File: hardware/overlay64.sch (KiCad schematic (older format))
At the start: 17 parts, among them IC1 ATMEGA328P-P, P1 ISP, P2 MAIN, P3 INPUT/BYPASS, Q1 BC547B, U1 LM1881, Y1 20MHz

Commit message: Hardware: Rearranged components, rerouting...
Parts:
- removed P3: INPUT/BYPASS, Pin_Headers:Pin_Header_Straight_2x14, symbol CONN_02X14
- added P3: CONTROL, Pin_Headers:Pin_Header_Angled_1x02, symbol CONN_01X02
- added P4: BYPASS, Pin_Headers:Pin_Header_Angled_1x12, symbol CONN_01X12
- added P5: INPUT, Pin_Headers:Pin_Header_Angled_1x12, symbol CONN_01X12
- P2: footprint Pin_Headers:Pin_Header_Straight_1x03 -> Pin_Headers:Pin_Header_Angled_1x03
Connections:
- net IN0: now also P4.1 (P1), P5.12 (P12)
- net IN1: now also P4.2 (P2), P5.11 (P11)
- net IN10: now also P4.11 (P11), P5.2 (P2)
- net IN11: now also P4.12 (P12), P5.1 (P1)
- net IN2: now also P4.3 (P3), P5.10 (P10)
- net IN3: now also P4.4 (P4), P5.9 (P9)
- net IN4: now also P4.5 (P5), P5.8 (P8)
- net IN5: now also P4.6 (P6), P5.7 (P7)
- net IN6: now also P4.7 (P7), P5.6 (P6)
- net IN7: now also P4.8 (P8), P5.5 (P5)
- net IN8: now also P4.9 (P9), P5.4 (P4)
- net IN9: now also P4.10 (P10), P5.3 (P3)
- net ~OE: now also P3.1 (P1)
- net ~OR: now also P3.2 (P2)
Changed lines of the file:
@@
 $EndComp
 $Comp
-L PWR_FLAG #FLG1
+L PWR_FLAG #FLG01
 U 1 1 56A1EF0B
 P 6250 7500
-F 0 "#FLG1" H 6250 7595 50  0001 C CNN
+F 0 "#FLG01" H 6250 7595 50  0001 C CNN
 F 1 "PWR_FLAG" H 6250 7680 50  0000 C CNN
 F 2 "" H 6250 7500 60  0000 C CNN
@@
 $EndComp
 $Comp
-L VCC #PWR12
+L VCC #PWR02
 U 1 1 56A1EF40
 P 6250 7500
-F 0 "#PWR12" H 6250 7350 50  0001 C CNN
+F 0 "#PWR02" H 6250 7350 50  0001 C CNN
 F 1 "VCC" H 6250 7650 50  0000 C CNN
 F 2 "" H 6250 7500 60  0000 C CNN
@@
 $EndComp
 $Comp
-L PWR_FLAG #FLG2
+L PWR_FLAG #FLG03
 U 1 1 56A1EF56
 P 6700 7500
-F 0 "#FLG2" H 6700 7595 50  0001 C CNN
+F 0 "#FLG03" H 6700 7595 50  0001 C CNN
 F 1 "PWR_FLAG" H 6700 7680 50  0000 C CNN
 F 2 "" H 6700 7500 60  0000 C CNN
@@
 $EndComp
 $Comp
-L GND #PWR15
+L GND #PWR04
 U 1 1 56A1EF6C
 P 6700 7500
-F 0 "#PWR15" H 6700 7250 50  0001 C CNN
+F 0 "#PWR04" H 6700 7250 50  0001 C CNN
 F 1 "GND" H 6700 7350 50  0000 C CNN
 F 2 "" H 6700 7500 60  0000 C CNN
@@
 $EndComp
 $Comp
-L VCC #PWR9
+L VCC #PWR05
 U 1 1 56A1F13D
 P 5600 4850
-F 0 "#PWR9" H 5600 4700 50  0001 C CNN
+F 0 "#PWR05" H 5600 4700 50  0001 C CNN
 F 1 "VCC" H 5600 5000 50  0000 C CNN
 F 2 "" H 5600 4850 60  0000 C CNN
@@
 $EndComp
 $Comp
-L GND #PWR10
+L GND #PWR06
 U 1 1 56A1F155
 P 5600 5150
-F 0 "#PWR10" H 5600 4900 50  0001 C CNN
+F 0 "#PWR06" H 5600 4900 50  0001 C CNN
 F 1 "GND" H 5600 5000 50  0000 C CNN
 F 2 "" H 5600 5150 60  0000 C CNN
@@
 $EndComp
 $Comp
-L GND #PWR2
+L GND #PWR07
 U 1 1 56A1F1BC
 P 2050 2800
-F 0 "#PWR2" H 2050 2550 50  0001 C CNN
+F 0 "#PWR07" H 2050 2550 50  0001 C CNN
 F 1 "GND" H 2050 2650 50  0000 C CNN
 F 2 "" H 2050 2800 60  0000 C CNN
@@
 $EndComp
 $Comp
-L GND #PWR16
+L GND #PWR08
 U 1 1 56A1F3BB
 P 6850 4350
-F 0 "#PWR16" H 6850 4100 50  0001 C CNN
+F 0 "#PWR08" H 6850 4100 50  0001 C CNN
 F 1 "GND" H 6850 4200 50  0000 C CNN
 F 2 "" H 6850 4350 60  0000 C CNN
@@
 $EndComp
 $Comp
-L VCC #PWR1
+L VCC #PWR09
 U 1 1 56A1FF3A
 P 2000 2500
-F 0 "#PWR1" H 2000 2350 50  0001 C CNN
+F 0 "#PWR09" H 2000 2350 50  0001 C CNN
 F 1 "VCC" H 2000 2650 50  0000 C CNN
 F 2 "" H 2000 2500 60  0000 C CNN
@@
 $EndComp
 $Comp
-L GND #PWR3
+L GND #PWR010
 U 1 1 56A20155
 P 2450 4700
-F 0 "#PWR3" H 2450 4450 50  0001 C CNN
+F 0 "#PWR010" H 2450 4450 50  0001 C CNN
 F 1 "GND" H 2450 4550 50  0000 C CNN
 F 2 "" H 2450 4700 60  0000 C CNN
@@
 $EndComp
 $Comp
-L GND #PWR4
+L GND #PWR011
 U 1 1 56A60DBD
 P 2450 4800
-F 0 "#PWR4" H 2450 4550 50  0001 C CNN
+F 0 "#PWR011" H 2450 4550 50  0001 C CNN
 F 1 "GND" H 2450 4650 50  0000 C CNN
 F 2 "" H 2450 4800 60  0000 C CNN
@@
 Connection ~ 6850 4350
 $Comp
-L VCC #PWR11
+L VCC #PWR012
 U 1 1 56A78618
 P 5800 2600
-F 0 "#PWR11" H 5800 2450 50  0001 C CNN
+F 0 "#PWR012" H 5800 2450 50  0001 C CNN
 F 1 "VCC" H 5800 2750 50  0000 C CNN
 F 2 "" H 5800 2600 60  0000 C CNN
@@
 MOSI
 $Comp
-L VCC #PWR5
+L VCC #PWR013
 U 1 1 56A92B5A
 P 3750 1750
-F 0 "#PWR5" H 3750 1600 50  0001 C CNN
+F 0 "#PWR013" H 3750 1600 50  0001 C CNN
 F 1 "VCC" H 3750 1900 50  0000 C CNN
 F 2 "" H 3750 1750 60  0000 C CNN
@@
 $EndComp
 $Comp
-L GND #PWR6
+L GND #PWR014
 U 1 1 56A92BBD
 P 3750 1950
-F 0 "#PWR6" H 3750 1700 50  0001 C CNN
+F 0 "#PWR014" H 3750 1700 50  0001 C CNN
 F 1 "GND" H 3750 1800 50  0000 C CNN
 F 2 "" H 3750 1950 60  0000 C CNN
@@
 $EndComp
 $Comp
-L GND #PWR7
+L GND #PWR015
 U 1 1 56A976F1
 P 4850 3050
-F 0 "#PWR7" H 4850 2800 50  0001 C CNN
+F 0 "#PWR015" H 4850 2800 50  0001 C CNN
 F 1 "GND" H 4850 2900 50  0000 C CNN
 F 2 "" H 4850 3050 60  0000 C CNN
@@
 $EndComp
 $Comp
-L GND #PWR8
+L GND #PWR016
 U 1 1 56A97733
 P 4850 3250
-F 0 "#PWR8" H 4850 3000 50  0001 C CNN
+F 0 "#PWR016" H 4850 3000 50  0001 C CNN
 F 1 "GND" H 4850 3100 50  0000 C CNN
 F 2 "" H 4850 3250 60  0000 C CNN
@@
 F 0 "P2" H 6650 3750 50  0000 C CNN
 F 1 "MAIN" V 6750 3550 50  0000 C CNN
-F 2 "Pin_Headers:Pin_Header_Straight_1x03" H 6650 3550 60  0001 C CNN
+F 2 "Pin_Headers:Pin_Header_Angled_1x03" H 6650 3550 60  0001 C CNN
 F 3 "" H 6650 3550 60  0000 C CNN
 	1    6650 3550
@@
 $EndComp
 $Comp
-L VCC #PWR13
+L VCC #PWR017
 U 1 1 56A9E7D0
 P 6450 3450
-F 0 "#PWR13" H 6450 3300 50  0001 C CNN
+F 0 "#PWR017" H 6450 3300 50  0001 C CNN
 F 1 "VCC" H 6450 3600 50  0000 C CNN
 F 2 "" H 6450 3450 60  0000 C CNN
@@
 $EndComp
 $Comp
-L GND #PWR14
+L GND #PWR018
 U 1 1 56A9E875
 P 6450 3650
-F 0 "#PWR14" H 6450 3400 50  0001 C CNN
+F 0 "#PWR018" H 6450 3400 50  0001 C CNN
 F 1 "GND" H 6450 3500 50  0000 C CNN
 F 2 "" H 6450 3650 60  0000 C CNN
@@
 Wire Wire Line
 	4750 4450 5300 4450
-Text Label 7750 3100 2    60   ~ 0
+Text Label 8700 3100 2    60   ~ 0
 IN0
-Text Label 7750 3200 2    60   ~ 0
+Text Label 8700 3200 2    60   ~ 0
 IN1
-Text Label 7750 3300 2    60   ~ 0
+Text Label 8700 3300 2    60   ~ 0
 IN2
-Text Label 7750 3400 2    60   ~ 0
+Text Label 8700 3400 2    60   ~ 0
 IN3
-Text Label 7750 3500 2    60   ~ 0
+Text Label 8700 3500 2    60   ~ 0
 IN4
-Text Label 7750 3600 2    60   ~ 0
+Text Label 8700 3600 2    60   ~ 0
 IN5
-Text Label 7750 3700 2    60   ~ 0
+Text Label 8700 3700 2    60   ~ 0
 IN6
-Text Label 7750 3800 2    60   ~ 0
+Text Label 8700 3800 2    60   ~ 0
 IN7
-Text Label 7750 3900 2    60   ~ 0
+Text Label 8700 3900 2    60   ~ 0
 IN8
-Text Label 7750 4000 2    60   ~ 0
+Text Label 8700 4000 2    60   ~ 0
 IN9
-Text Label 7750 4100 2    60   ~ 0
+Text Label 8700 4100 2    60   ~ 0
 IN10
-Text Label 7750 4200 2    60   ~ 0
+Text Label 8700 4200 2    60   ~ 0
 IN11
 $Comp
@@
 Text Label 4350 4800 0    60   ~ 0
 ~OR
-Text Label 7750 4300 2    60   ~ 0
+Text Label 4300 6150 2    60   ~ 0
 ~OE
 Text Label 6150 3550 0    60   ~ 0
 LUMA
-$Comp
-L CONN_02X14 P3
-U 1 1 56B0DCD2
-P 8000 3750
-F 0 "P3" H 8000 4500 50  0000 C CNN
-F 1 "INPUT/BYPASS" V 8000 3750 50  0000 C CNN
-F 2 "Pin_Headers:Pin_Header_Straight_2x14" H 8000 2600 60  0001 C CNN
-F 3 "" H 8000 2600 60  0000 C CNN
-	1    8000 3750
-	1    0    0    -1
-$EndComp
-Text Label 8250 4300 0    60   ~ 0
-~OE
-Text Label 8250 3100 0    60   ~ 0
+Text Label 7850 3150 2    60   ~ 0
 IN0
-Text Label 8250 3200 0    60   ~ 0
+Text Label 7850 3250 2    60   ~ 0
 IN1
-Text Label 8250 3300 0    60   ~ 0
+Text Label 7850 3350 2    60   ~ 0
 IN2
-Text Label 8250 3400 0    60   ~ 0
+Text Label 7850 3450 2    60   ~ 0
 IN3
-Text Label 8250 3500 0    60   ~ 0
+Text Label 7850 3550 2    60   ~ 0
 IN4
-Text Label 8250 3600 0    60   ~ 0
+Text Label 7850 3650 2    60   ~ 0
 IN5
-Text Label 8250 3700 0    60   ~ 0
+Text Label 7850 3750 2    60   ~ 0
 IN6
-Text Label 8250 3800 0    60   ~ 0
+Text Label 7850 3850 2    60   ~ 0
 IN7
-Text Label 8250 3900 0    60   ~ 0
+Text Label 7850 3950 2    60   ~ 0
 IN8
-Text Label 8250 4000 0    60   ~ 0
+Text Label 7850 4050 2    60   ~ 0
 IN9
-Text Label 8250 4100 0    60   ~ 0
+Text Label 7850 4150 2    60   ~ 0
 IN10
-Text Label 8250 4200 0    60   ~ 0
+Text Label 7850 4250 2    60   ~ 0
 IN11
 $Comp
@@
 Text Label 4350 4700 0    60   ~ 0
 ~OE
-Text Label 8250 4400 0    60   ~ 0
+Text Label 4300 6250 2    60   ~ 0
 ~OR
-Text Label 7750 4400 2    60   ~ 0
-~OR
+$Comp
+L CONN_01X12 P4
+U 1 1 572F57F1
+P 8900 3650
+F 0 "P4" H 8900 4300 50  0000 C CNN
+F 1 "BYPASS" V 9000 3650 50  0000 C CNN
+F 2 "Pin_Headers:Pin_Header_Angled_1x12" H 8900 3650 50  0001 C CNN
+F 3 "" H 8900 3650 50  0000 C CNN
+	1    8900 3650
+	1    0    0    -1
+$EndComp
+$Comp
+L CONN_01X12 P5
+U 1 1 572F58A5
+P 8050 3700
+F 0 "P5" H 8050 4350 50  0000 C CNN
+F 1 "INPUT" V 8150 3700 50  0000 C CNN
+F 2 "Pin_Headers:Pin_Header_Angled_1x12" H 8050 3700 50  0001 C CNN
+F 3 "" H 8050 3700 50  0000 C CNN
+	1    8050 3700
+	1    0    0    1
+$EndComp
+$Comp
+L CONN_01X02 P3
+U 1 1 572F59E5
+P 4500 6200
+F 0 "P3" H 4500 6350 50  0000 C CNN
+F 1 "CONTROL" V 4600 6200 50  0000 C CNN
+F 2 "Pin_Headers:Pin_Header_Angled_1x02" H 4500 6200 50  0001 C CNN
+F 3 "" H 4500 6200 50  0000 C CNN
+	1    4500 6200
+	1    0    0    -1
+$EndComp
 $EndSCHEMATC

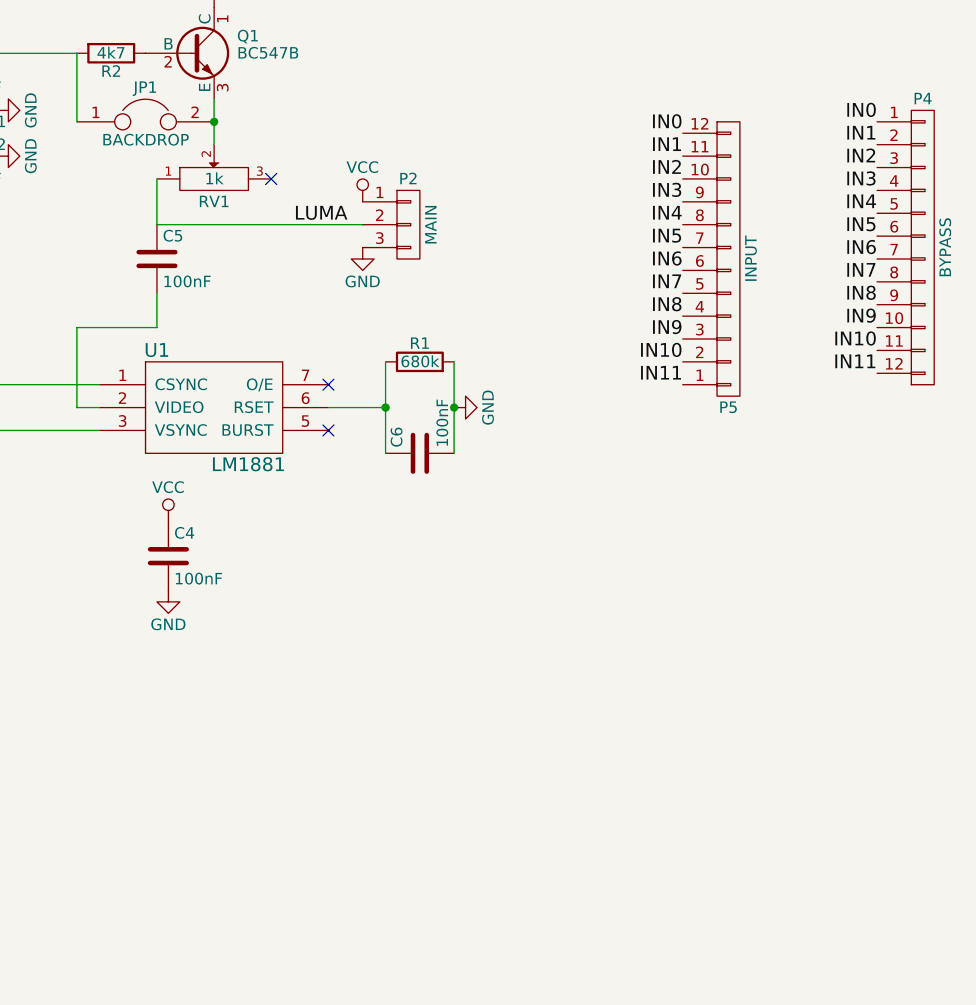
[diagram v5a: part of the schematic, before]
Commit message: Hardware: Fixed orientation/wiring for brightness pot
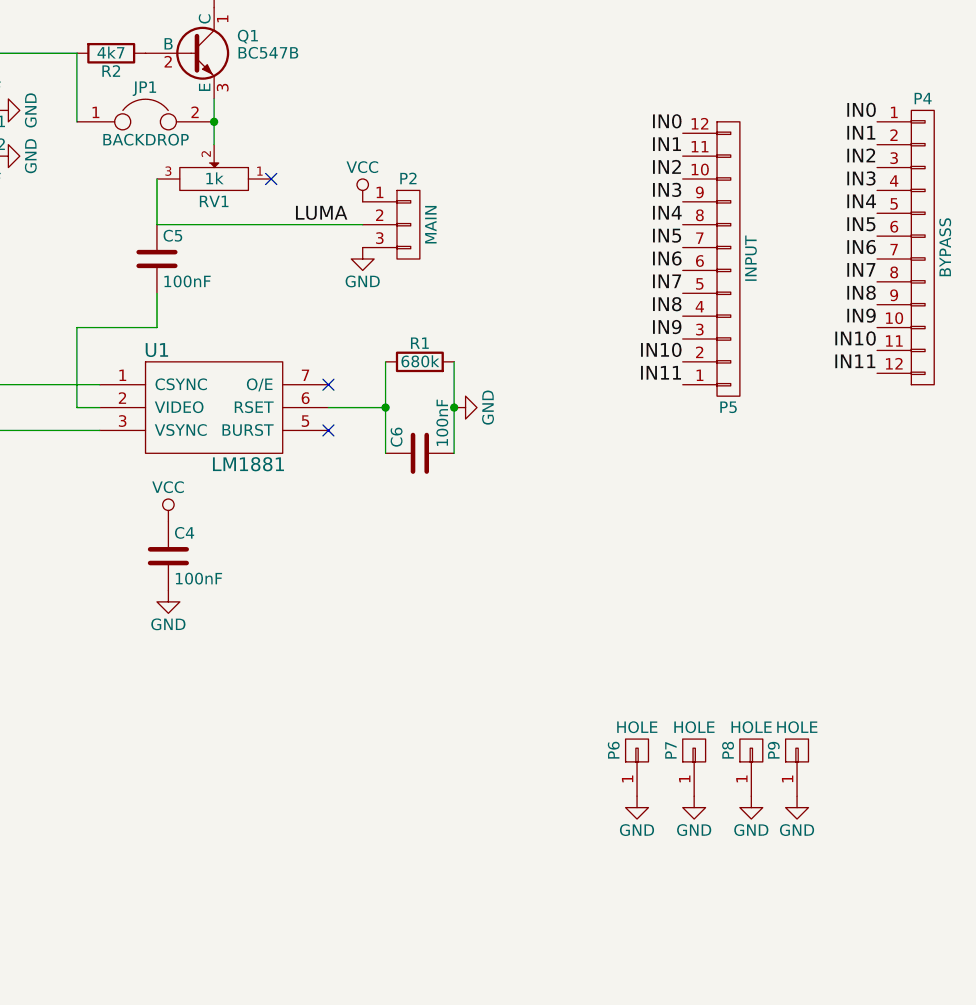
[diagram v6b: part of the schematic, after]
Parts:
- added P6, P7, P8, P9: HOLE, Mounting_Holes:MountingHole_4mm, symbol CONN_01X01
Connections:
- net GND: now also P6.1 (P1), P7.1 (P1), P8.1 (P1), P9.1 (P1)
- net LUMA: now also RV1.3; no longer RV1.1
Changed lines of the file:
@@
 F 3 "" H 5800 3350 60  0000 C CNN
 	1    5800 3350
-	1    0    0    -1
+	-1   0    0    -1
 $EndComp
 NoConn ~ 6050 3350
@@
 	1    0    0    -1
 $EndComp
+$Comp
+L CONN_01X01 P6
+U 1 1 57445960
+P 7650 5850
+F 0 "P6" H 7650 5950 50  0000 C CNN
+F 1 "HOLE" V 7750 5850 50  0000 C CNN
+F 2 "Mounting_Holes:MountingHole_4mm" H 7650 5850 60  0001 C CNN
+F 3 "" H 7650 5850 60  0000 C CNN
+	1    7650 5850
+	0    -1   -1   0
+$EndComp
+$Comp
+L CONN_01X01 P7
+U 1 1 57445B56
+P 7900 5850
+F 0 "P7" H 7900 5950 50  0000 C CNN
+F 1 "HOLE" V 8000 5850 50  0000 C CNN
+F 2 "Mounting_Holes:MountingHole_4mm" H 7900 5850 60  0001 C CNN
+F 3 "" H 7900 5850 60  0000 C CNN
+	1    7900 5850
+	0    -1   -1   0
+$EndComp
+$Comp
+L CONN_01X01 P8
+U 1 1 57445BAB
+P 8150 5850
+F 0 "P8" H 8150 5950 50  0000 C CNN
+F 1 "HOLE" V 8250 5850 50  0000 C CNN
+F 2 "Mounting_Holes:MountingHole_4mm" H 8150 5850 60  0001 C CNN
+F 3 "" H 8150 5850 60  0000 C CNN
+	1    8150 5850
+	0    -1   -1   0
+$EndComp
+$Comp
+L CONN_01X01 P9
+U 1 1 57445C03
+P 8350 5850
+F 0 "P9" H 8350 5950 50  0000 C CNN
+F 1 "HOLE" V 8450 5850 50  0000 C CNN
+F 2 "Mounting_Holes:MountingHole_4mm" H 8350 5850 60  0001 C CNN
+F 3 "" H 8350 5850 60  0000 C CNN
+	1    8350 5850
+	0    -1   -1   0
+$EndComp
+$Comp
+L GND #PWR019
+U 1 1 57445C4B
+P 7650 6050
+F 0 "#PWR019" H 7650 5800 50  0001 C CNN
+F 1 "GND" H 7650 5900 50  0000 C CNN
+F 2 "" H 7650 6050 60  0000 C CNN
+F 3 "" H 7650 6050 60  0000 C CNN
+	1    7650 6050
+	1    0    0    -1
+$EndComp
+$Comp
+L GND #PWR020
+U 1 1 57445CA2
+P 7900 6050
+F 0 "#PWR020" H 7900 5800 50  0001 C CNN
+F 1 "GND" H 7900 5900 50  0000 C CNN
+F 2 "" H 7900 6050 60  0000 C CNN
+F 3 "" H 7900 6050 60  0000 C CNN
+	1    7900 6050
+	1    0    0    -1
+$EndComp
+$Comp
+L GND #PWR021
+U 1 1 57445CF2
+P 8150 6050
+F 0 "#PWR021" H 8150 5800 50  0001 C CNN
+F 1 "GND" H 8150 5900 50  0000 C CNN
+F 2 "" H 8150 6050 60  0000 C CNN
+F 3 "" H 8150 6050 60  0000 C CNN
+	1    8150 6050
+	1    0    0    -1
+$EndComp
+$Comp
+L GND #PWR022
+U 1 1 57445D42
+P 8350 6050
+F 0 "#PWR022" H 8350 5800 50  0001 C CNN
+F 1 "GND" H 8350 5900 50  0000 C CNN
+F 2 "" H 8350 6050 60  0000 C CNN
+F 3 "" H 8350 6050 60  0000 C CNN
+	1    8350 6050
+	1    0    0    -1
+$EndComp
